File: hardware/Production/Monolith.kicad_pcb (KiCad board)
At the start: 6 copper layers, 43.2 x 74.4 mm, 289 parts, among them J102 Cell 1 NTC wires, J105 Cell 2 NTC wires, J106 Cell 3 NTC wires, J107 Cell 4 NTC wires, J108 PACK- power wire, J109 CELL1 sense wire, J110 CELL2 sense wire, J111 CELL3 sense wire, J112 PACK+ power wire, J113 LOAD PACK_P, J114 LOAD GND, J115 1N Kelvin wire, J116 4P Kelvin wire, J301 TC2030-NL, J302 TC2030-NL GAUGE, J401 TYPE-C 16PCB1.6 IP68, J501 TYPE-C 16PCB1.6 IP68, Q101 AGM404AP1, Q102 AGM404AP1, Q103 AO3400A, Q104 AO3400A, Q401 SiZ240DT, Q402 SiZ240DT, Q501 SiZ240DT, Q502 SiZ240DT, U101 BQ40Z50RSMR-R2, U102 BQ294700DSGR, U204 TPS62177DQCR, U301 CC2340R5MODA, U401 TPS25751DREFR, U402 M24512-DFMC6TG, U403 BQ25756RRVR, U404 TPS62933DRLR, U405 TPD6S300RUKR, U501 TPS25751DREFR, U502 M24512-DFMC6TG, U503 BQ25756RRVR, U504 TPS62933DRLR, U505 TPD6S300RUKR

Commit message: Sense pads 1.5 x 1.4: clear the USB-C courtyards and match the library
DRC flagged J109 / J111 courtyards overlapping J501 / J401 (the 4.2 mm oval
pads kept from the old tab slots) and all five sense footprints as not
matching the library (the board copies still had the slot outline on F.Fab).
Nothing is routed to them yet, so every sense pad is now Ø0.8 in a 1.5 x 1.4
pad (SB_SWIRE_PAD_L), one library footprint, with the board copies written
to match it. J109 / J111 courtyards end 0.05 mm short of the USB-C ones.

Co-Authored-By: Claude Opus 5.5 (1M context) <noreply@anthropic.com>
Claude-Session: https://claude.ai/code/session_01V2XuchjL8SPbkwDuzZLoSy
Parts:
- J109, J110, J111: footprint MonolithDev:SolderWire-28AWG_PTFE_1x01_D0.8mm_Pad4.2x1.4mm -> MonolithDev:SolderWire-28AWG_PTFE_1x01_D0.8mm_Pad1.5x1.4mm
- J115, J116: footprint MonolithDev:SolderWire-28AWG_PTFE_1x01_D0.8mm_Pad2.4x1.4mm -> MonolithDev:SolderWire-28AWG_PTFE_1x01_D0.8mm_Pad1.5x1.4mm
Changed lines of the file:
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@@
 		)
 	)
-	(footprint "MonolithDev:SolderWire-28AWG_PTFE_1x01_D0.8mm_Pad2.4x1.4mm"
+	(footprint "MonolithDev:SolderWire-28AWG_PTFE_1x01_D0.8mm_Pad1.5x1.4mm"
 		(locked yes)
 		(layer "F.Cu")
 		(at 91.275 135.4755)
-		(descr "Plated hole 0.8 mm in a 2.4 x 1.4 mm pad, for a 28 AWG PTFE sense wire soldered on F.Cu (mechanical/monolith_shell.py sb_slots)")
+		(descr "Plated hole 0.8 mm in a 1.5 x 1.4 mm pad, for a 28 AWG PTFE sense wire soldered on F.Cu (mechanical/monolith_shell.py sb_slots)")
 		(tags "connector wire 28AWG PTFE battery sense")
 		(property "Reference" "J115"
@@
 		(duplicate_pad_numbers_are_jumpers no)
 		(fp_rect
-			(start -1.3 -0.8)
-			(end 1.3 0.8)
+			(start -0.85 -0.8)
+			(end 0.85 0.8)
 			(stroke
 				(width 0.05)
@@
 			(layer "F.CrtYd")
 		)
-		(fp_rect
-			(start -0.8 -0.3)
-			(end 0.8 0.3)
+		(fp_circle
+			(center 0 0)
+			(end 0.375 0)
 			(stroke
 				(width 0.1)
@@
 		(pad "1" thru_hole oval
 			(at 0 0)
-			(size 2.4 1.4)
+			(size 1.5 1.4)
 			(drill 0.8)
 			(layers "*.Cu" "*.Mask")
@@
 		)
 	)
-	(footprint "MonolithDev:SolderWire-28AWG_PTFE_1x01_D0.8mm_Pad4.2x1.4mm"
+	(footprint "MonolithDev:SolderWire-28AWG_PTFE_1x01_D0.8mm_Pad1.5x1.4mm"
 		(locked yes)
 		(layer "F.Cu")
 		(at 100 135.4505)
-		(descr "Plated hole 0.8 mm in a 4.2 x 1.4 mm pad, for a 28 AWG PTFE sense wire soldered on F.Cu (mechanical/monolith_shell.py sb_slots)")
+		(descr "Plated hole 0.8 mm in a 1.5 x 1.4 mm pad, for a 28 AWG PTFE sense wire soldered on F.Cu (mechanical/monolith_shell.py sb_slots)")
 		(tags "connector wire 28AWG PTFE battery sense")
 		(property "Reference" "J110"
@@
 		(duplicate_pad_numbers_are_jumpers no)
 		(fp_rect
-			(start -2.2 -0.8)
-			(end 2.2 0.8)
+			(start -0.85 -0.8)
+			(end 0.85 0.8)
 			(stroke
 				(width 0.05)
@@
 			(layer "F.CrtYd")
 		)
-		(fp_rect
-			(start -1.7 -0.3)
-			(end 1.7 0.3)
+		(fp_circle
+			(center 0 0)
+			(end 0.375 0)
 			(stroke
 				(width 0.1)
@@
 		(pad "1" thru_hole oval
 			(at 0 0)
-			(size 4.2 1.4)
+			(size 1.5 1.4)
 			(drill 0.8)
 			(layers "*.Cu" "*.Mask")
@@
 		)
 	)
-	(footprint "MonolithDev:SolderWire-28AWG_PTFE_1x01_D0.8mm_Pad4.2x1.4mm"
+	(footprint "MonolithDev:SolderWire-28AWG_PTFE_1x01_D0.8mm_Pad1.5x1.4mm"
 		(locked yes)
 		(layer "F.Cu")
 		(at 113.9 69.4755)
-		(descr "Plated hole 0.8 mm in a 4.2 x 1.4 mm pad, for a 28 AWG PTFE sense wire soldered on F.Cu (mechanical/monolith_shell.py sb_slots)")
+		(descr "Plated hole 0.8 mm in a 1.5 x 1.4 mm pad, for a 28 AWG PTFE sense wire soldered on F.Cu (mechanical/monolith_shell.py sb_slots)")
 		(tags "connector wire 28AWG PTFE battery sense")
 		(property "Reference" "J111"
@@
 		(duplicate_pad_numbers_are_jumpers no)
 		(fp_rect
-			(start -2.2 -0.8)
-			(end 2.2 0.8)
+			(start -0.85 -0.8)
+			(end 0.85 0.8)
 			(stroke
 				(width 0.05)
@@
 			(layer "F.CrtYd")
 		)
-		(fp_rect
-			(start -1.7 -0.3)
-			(end 1.7 0.3)
+		(fp_circle
+			(center 0 0)
+			(end 0.375 0)
 			(stroke
 				(width 0.1)
@@
 		(pad "1" thru_hole oval
 			(at 0 0)
-			(size 4.2 1.4)
+			(size 1.5 1.4)
 			(drill 0.8)
 			(layers "*.Cu" "*.Mask")
@@
 		)
 	)
-	(footprint "MonolithDev:SolderWire-28AWG_PTFE_1x01_D0.8mm_Pad4.2x1.4mm"
+	(footprint "MonolithDev:SolderWire-28AWG_PTFE_1x01_D0.8mm_Pad1.5x1.4mm"
 		(locked yes)
 		(layer "F.Cu")
 		(at 86.1 69.4755)
-		(descr "Plated hole 0.8 mm in a 4.2 x 1.4 mm pad, for a 28 AWG PTFE sense wire soldered on F.Cu (mechanical/monolith_shell.py sb_slots)")
+		(descr "Plated hole 0.8 mm in a 1.5 x 1.4 mm pad, for a 28 AWG PTFE sense wire soldered on F.Cu (mechanical/monolith_shell.py sb_slots)")
 		(tags "connector wire 28AWG PTFE battery sense")
 		(property "Reference" "J109"
@@
 		(duplicate_pad_numbers_are_jumpers no)
 		(fp_rect
-			(start -2.2 -0.8)
-			(end 2.2 0.8)
+			(start -0.85 -0.8)
+			(end 0.85 0.8)
 			(stroke
 				(width 0.05)
@@
 			(layer "F.CrtYd")
 		)
-		(fp_rect
-			(start -1.7 -0.3)
-			(end 1.7 0.3)
+		(fp_circle
+			(center 0 0)
+			(end 0.375 0)
 			(stroke
 				(width 0.1)
@@
 		(pad "1" thru_hole oval
 			(at 0 0)
-			(size 4.2 1.4)
+			(size 1.5 1.4)
 			(drill 0.8)
 			(layers "*.Cu" "*.Mask")
@@
 		)
 	)
-	(footprint "MonolithDev:SolderWire-28AWG_PTFE_1x01_D0.8mm_Pad2.4x1.4mm"
+	(footprint "MonolithDev:SolderWire-28AWG_PTFE_1x01_D0.8mm_Pad1.5x1.4mm"
 		(locked yes)
 		(layer "F.Cu")
 		(at 108.725 135.4755)
-		(descr "Plated hole 0.8 mm in a 2.4 x 1.4 mm pad, for a 28 AWG PTFE sense wire soldered on F.Cu (mechanical/monolith_shell.py sb_slots)")
+		(descr "Plated hole 0.8 mm in a 1.5 x 1.4 mm pad, for a 28 AWG PTFE sense wire soldered on F.Cu (mechanical/monolith_shell.py sb_slots)")
 		(tags "connector wire 28AWG PTFE battery sense")
 		(property "Reference" "J116"
@@
 		(duplicate_pad_numbers_are_jumpers no)
 		(fp_rect
-			(start -1.3 -0.8)
-			(end 1.3 0.8)
+			(start -0.85 -0.8)
+			(end 0.85 0.8)
 			(stroke
 				(width 0.05)
@@
 			(layer "F.CrtYd")
 		)
-		(fp_rect
-			(start -0.8 -0.3)
-			(end 0.8 0.3)
+		(fp_circle
+			(center 0 0)
+			(end 0.375 0)
 			(stroke
 				(width 0.1)
@@
 		(pad "1" thru_hole oval
 			(at 0 0)
-			(size 2.4 1.4)
+			(size 1.5 1.4)
 			(drill 0.8)
 			(layers "*.Cu" "*.Mask")

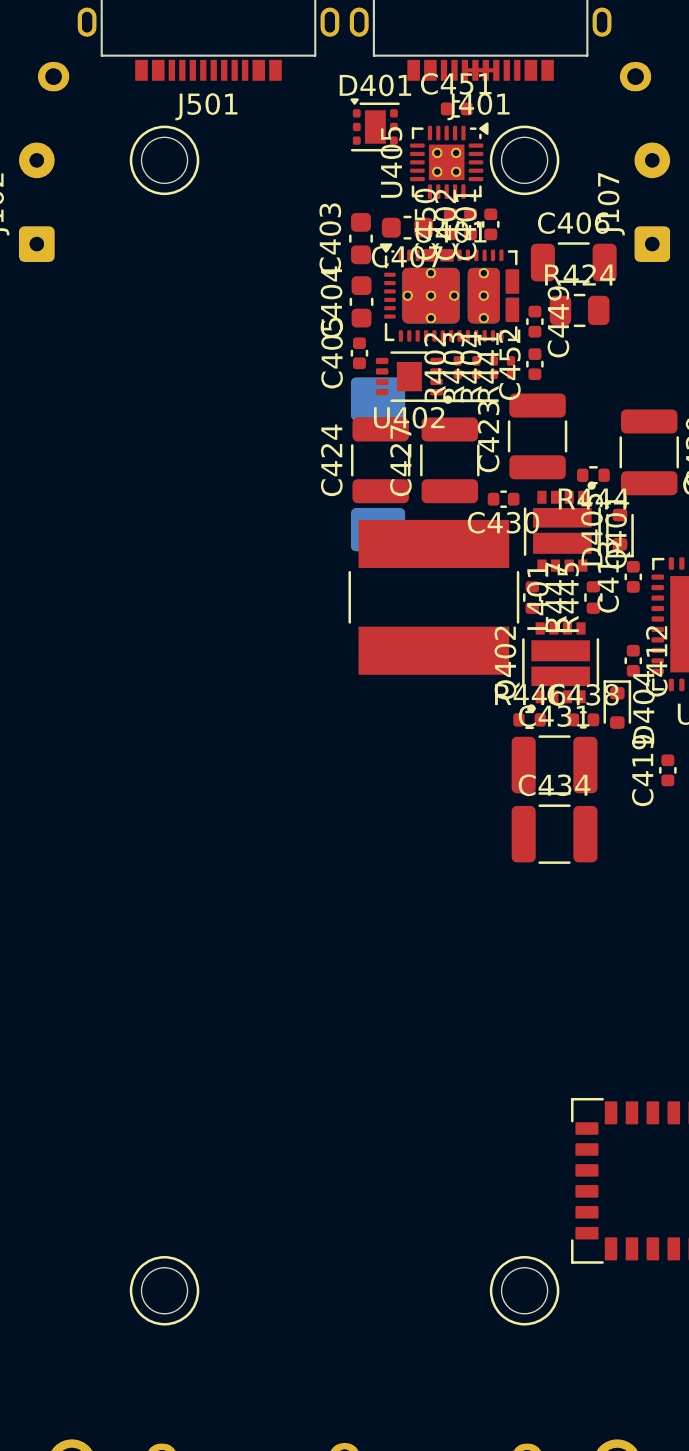
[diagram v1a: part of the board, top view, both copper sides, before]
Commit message: Peg holes to 2.6 x 2.2 slots so the USB-C seal bores centre the ports
The four carrier peg holes (H101-H104) were Ø2.2 for Ø2.0 pegs, so the
pegs, not the seal bores, set where the USB-C rings sit. They are now
2.6 x 2.2 NPTH slots, long across the board: +-0.3 float in y lets the
bores' 0.3 lead-in centre the rings along their long side, and +-0.1 in
z keeps a cable push from sliding the board down and pulling the rings
out of the top wall. The Ø4 TPU sleeves still cover the slots at full
float, and the board-face wall sits 0.5 over them.

- monolith_shell: CUP_PEG_SLOT replaces CUP_PEG_HOLE_D
- monolith_cup: checks for the float, ring depth and sleeve cover
- make_production: peg_footprint() draws the slot; new library footprint
  Peg_NPTH_Slot2.6x2.2mm, old D2.2 removed; board copies and schematic
  fields match it
- docs: p0-assembly and README; flags U405 pins 2.0 mm from H104 (the
  sleeve lands on them, and the bigger courtyard overlaps U405's)

Co-Authored-By: Claude Opus 5.5 (1M context) <noreply@anthropic.com>
Claude-Session: https://claude.ai/code/session_01V2XuchjL8SPbkwDuzZLoSy
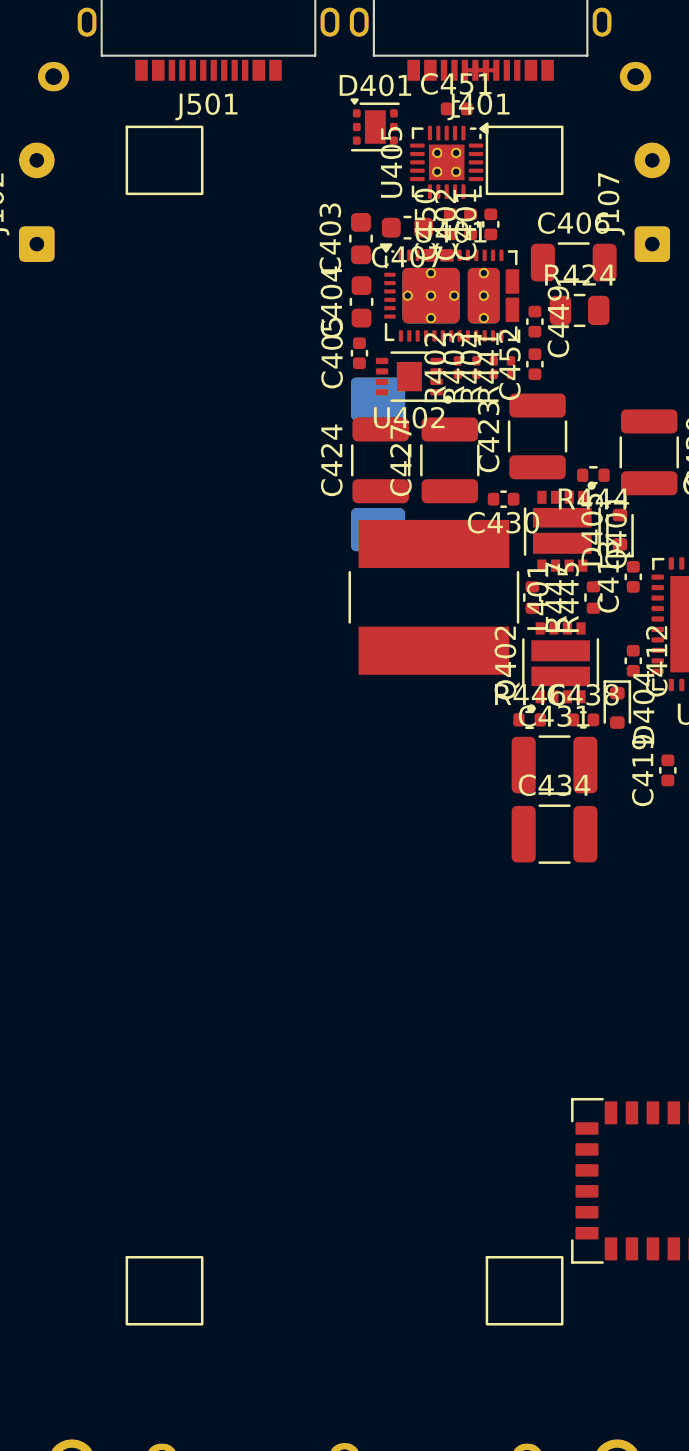
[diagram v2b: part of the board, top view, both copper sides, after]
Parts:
- H101, H102, H103, H104: value Peg hole 2.2 NPTH -> Peg slot 2.6x2.2 NPTH; footprint MonolithDev:Peg_NPTH_D2.2mm -> MonolithDev:Peg_NPTH_Slot2.6x2.2mm
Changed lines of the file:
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@@
 		)
 	)
-	(footprint "MonolithDev:Peg_NPTH_D2.2mm"
+	(footprint "MonolithDev:Peg_NPTH_Slot2.6x2.2mm"
 		(locked yes)
 		(layer "F.Cu")
 		(at 108.6 73.4755)
-		(descr "NPTH 2.2 mm for a 2 mm PA12 carrier peg (mechanical/monolith_cup.py)")
-		(tags "peg hole npth")
+		(descr "NPTH 2.6 x 2.2 mm slot for a 2 mm PA12 carrier peg (mechanical/monolith_cup.py)")
+		(tags "peg slot npth")
 		(property "Reference" "H104"
 			(at 0 -2.2 0)
@@
 			)
 		)
-		(property "Value" "Peg hole 2.2 NPTH"
+		(property "Value" "Peg slot 2.6x2.2 NPTH"
 			(at 0 2.2 0)
 			(layer "F.Fab")
@@
 		(attr exclude_from_pos_files exclude_from_bom)
 		(duplicate_pad_numbers_are_jumpers no)
-		(fp_circle
-			(center 0 0)
-			(end 1.6 0)
+		(fp_rect
+			(start -1.8 -1.6)
+			(end 1.8 1.6)
 			(stroke
 				(width 0.12)
@@
 			(layer "F.SilkS")
 		)
-		(fp_circle
-			(center 0 0)
-			(end 1.6 0)
+		(fp_rect
+			(start -1.8 -1.6)
+			(end 1.8 1.6)
 			(stroke
 				(width 0.05)
@@
 			(layer "B.CrtYd")
 		)
-		(fp_circle
-			(center 0 0)
-			(end 1.6 0)
+		(fp_rect
+			(start -1.8 -1.6)
+			(end 1.8 1.6)
 			(stroke
 				(width 0.05)
@@
 			(layer "F.CrtYd")
 		)
-		(pad "" np_thru_hole circle
+		(pad "" np_thru_hole oval
 			(at 0 0)
-			(size 2.2 2.2)
-			(drill 2.2)
+			(size 2.6 2.2)
+			(drill oval 2.6 2.2)
 			(layers "*.Cu" "*.Mask")
 		)
@@
 		)
 	)
-	(footprint "MonolithDev:Peg_NPTH_D2.2mm"
+	(footprint "MonolithDev:Peg_NPTH_Slot2.6x2.2mm"
 		(locked yes)
 		(layer "F.Cu")
 		(at 91.4 73.4755)
-		(descr "NPTH 2.2 mm for a 2 mm PA12 carrier peg (mechanical/monolith_cup.py)")
-		(tags "peg hole npth")
+		(descr "NPTH 2.6 x 2.2 mm slot for a 2 mm PA12 carrier peg (mechanical/monolith_cup.py)")
+		(tags "peg slot npth")
 		(property "Reference" "H102"
 			(at 0 -2.2 0)
@@
 			)
 		)
-		(property "Value" "Peg hole 2.2 NPTH"
+		(property "Value" "Peg slot 2.6x2.2 NPTH"
 			(at 0 2.2 0)
 			(layer "F.Fab")
@@
 		(attr exclude_from_pos_files exclude_from_bom)
 		(duplicate_pad_numbers_are_jumpers no)
-		(fp_circle
-			(center 0 0)
-			(end 1.6 0)
+		(fp_rect
+			(start -1.8 -1.6)
+			(end 1.8 1.6)
 			(stroke
 				(width 0.12)
@@
 			(layer "F.SilkS")
 		)
-		(fp_circle
-			(center 0 0)
-			(end 1.6 0)
+		(fp_rect
+			(start -1.8 -1.6)
+			(end 1.8 1.6)
 			(stroke
 				(width 0.05)
@@
 			(layer "B.CrtYd")
 		)
-		(fp_circle
-			(center 0 0)
-			(end 1.6 0)
+		(fp_rect
+			(start -1.8 -1.6)
+			(end 1.8 1.6)
 			(stroke
 				(width 0.05)
@@
 			(layer "F.CrtYd")
 		)
-		(pad "" np_thru_hole circle
+		(pad "" np_thru_hole oval
 			(at 0 0)
-			(size 2.2 2.2)
-			(drill 2.2)
+			(size 2.6 2.2)
+			(drill oval 2.6 2.2)
 			(layers "*.Cu" "*.Mask")
 		)
@@
 		)
 	)
-	(footprint "MonolithDev:Peg_NPTH_D2.2mm"
+	(footprint "MonolithDev:Peg_NPTH_Slot2.6x2.2mm"
 		(locked yes)
 		(layer "F.Cu")
 		(at 108.6 127.4755)
-		(descr "NPTH 2.2 mm for a 2 mm PA12 carrier peg (mechanical/monolith_cup.py)")
-		(tags "peg hole npth")
+		(descr "NPTH 2.6 x 2.2 mm slot for a 2 mm PA12 carrier peg (mechanical/monolith_cup.py)")
+		(tags "peg slot npth")
 		(property "Reference" "H103"
 			(at 0 -2.2 0)
@@
 			)
 		)
-		(property "Value" "Peg hole 2.2 NPTH"
+		(property "Value" "Peg slot 2.6x2.2 NPTH"
 			(at 0 2.2 0)
 			(layer "F.Fab")
@@
 		(attr exclude_from_pos_files exclude_from_bom)
 		(duplicate_pad_numbers_are_jumpers no)
-		(fp_circle
-			(center 0 0)
-			(end 1.6 0)
+		(fp_rect
+			(start -1.8 -1.6)
+			(end 1.8 1.6)
 			(stroke
 				(width 0.12)
@@
 			(layer "F.SilkS")
 		)
-		(fp_circle
-			(center 0 0)
-			(end 1.6 0)
+		(fp_rect
+			(start -1.8 -1.6)
+			(end 1.8 1.6)
 			(stroke
 				(width 0.05)
@@
 			(layer "B.CrtYd")
 		)
-		(fp_circle
-			(center 0 0)
-			(end 1.6 0)
+		(fp_rect
+			(start -1.8 -1.6)
+			(end 1.8 1.6)
 			(stroke
 				(width 0.05)
@@
 			(layer "F.CrtYd")
 		)
-		(pad "" np_thru_hole circle
+		(pad "" np_thru_hole oval
 			(at 0 0)
-			(size 2.2 2.2)
-			(drill 2.2)
+			(size 2.6 2.2)
+			(drill oval 2.6 2.2)
 			(layers "*.Cu" "*.Mask")
 		)
@@
 		)
 	)
-	(footprint "MonolithDev:Peg_NPTH_D2.2mm"
+	(footprint "MonolithDev:Peg_NPTH_Slot2.6x2.2mm"
 		(locked yes)
 		(layer "F.Cu")
 		(at 91.4 127.4755)
-		(descr "NPTH 2.2 mm for a 2 mm PA12 carrier peg (mechanical/monolith_cup.py)")
-		(tags "peg hole npth")
+		(descr "NPTH 2.6 x 2.2 mm slot for a 2 mm PA12 carrier peg (mechanical/monolith_cup.py)")
+		(tags "peg slot npth")
 		(property "Reference" "H101"
 			(at 0 -2.2 0)
@@
 			)
 		)
-		(property "Value" "Peg hole 2.2 NPTH"
+		(property "Value" "Peg slot 2.6x2.2 NPTH"
 			(at 0 2.2 0)
 			(layer "F.Fab")
@@
 		(attr exclude_from_pos_files exclude_from_bom)
 		(duplicate_pad_numbers_are_jumpers no)
-		(fp_circle
-			(center 0 0)
-			(end 1.6 0)
+		(fp_rect
+			(start -1.8 -1.6)
+			(end 1.8 1.6)
 			(stroke
 				(width 0.12)
@@
 			(layer "F.SilkS")
 		)
-		(fp_circle
-			(center 0 0)
-			(end 1.6 0)
+		(fp_rect
+			(start -1.8 -1.6)
+			(end 1.8 1.6)
 			(stroke
 				(width 0.05)
@@
 			(layer "B.CrtYd")
 		)
-		(fp_circle
-			(center 0 0)
-			(end 1.6 0)
+		(fp_rect
+			(start -1.8 -1.6)
+			(end 1.8 1.6)
 			(stroke
 				(width 0.05)
@@
 			(layer "F.CrtYd")
 		)
-		(pad "" np_thru_hole circle
+		(pad "" np_thru_hole oval
 			(at 0 0)
-			(size 2.2 2.2)
-			(drill 2.2)
+			(size 2.6 2.2)
+			(drill oval 2.6 2.2)
 			(layers "*.Cu" "*.Mask")
 		)
